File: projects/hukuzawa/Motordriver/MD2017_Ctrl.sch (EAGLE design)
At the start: 18 parts, among them IC1 PIC16F648, J1 3X2A, Q1 CERALOCK

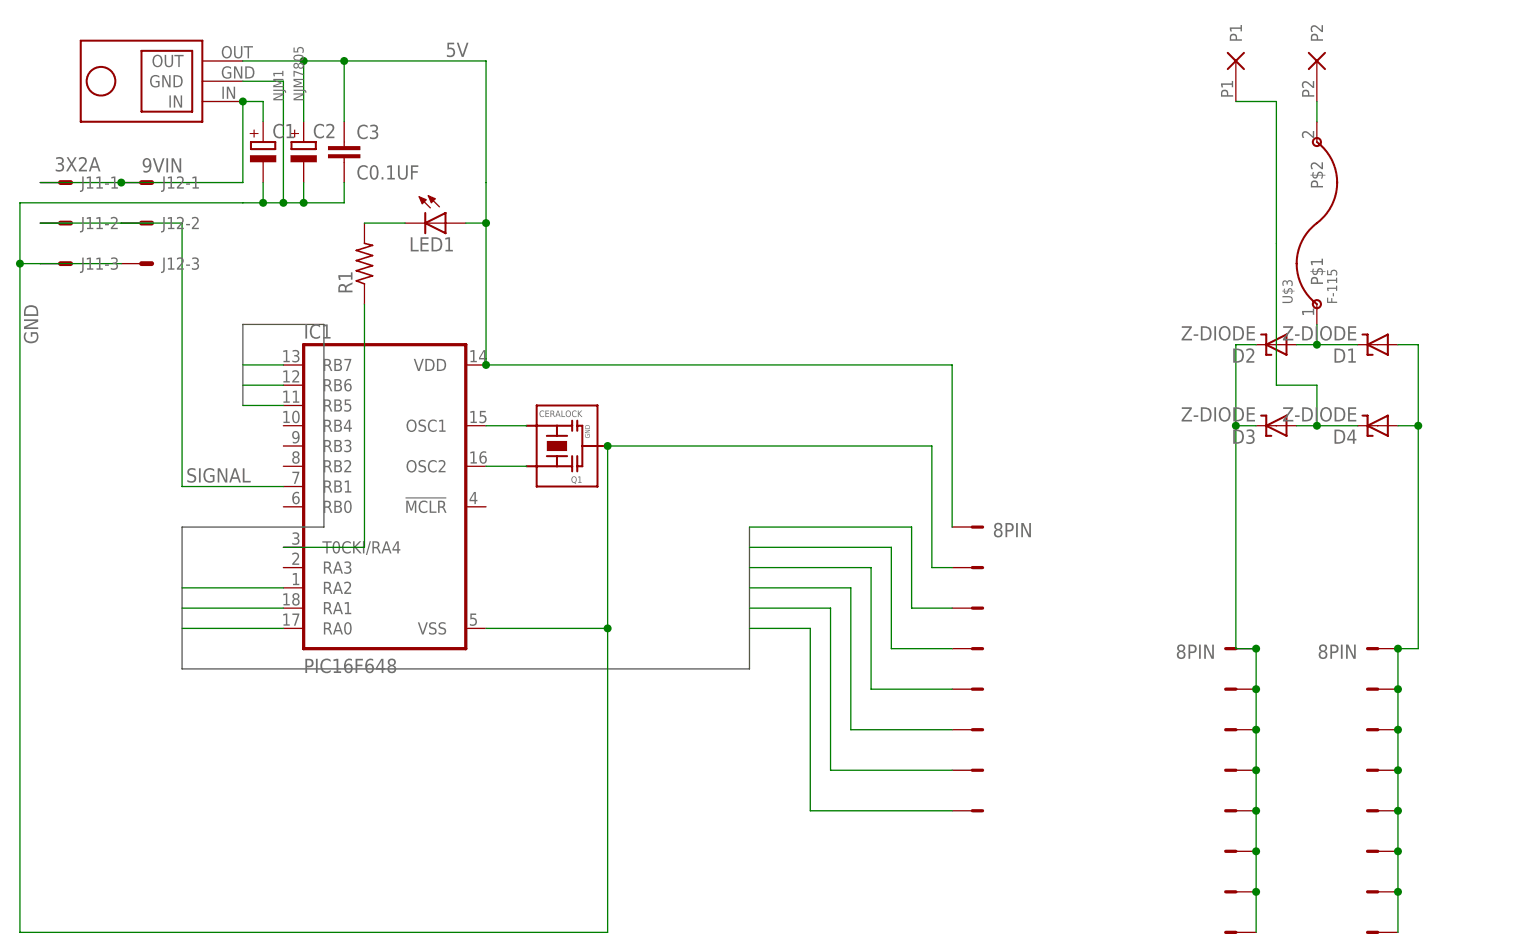
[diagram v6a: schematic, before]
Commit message: モータードライバ全ボード図修正
配置の基準単位をmilに変更して再配置・再配線
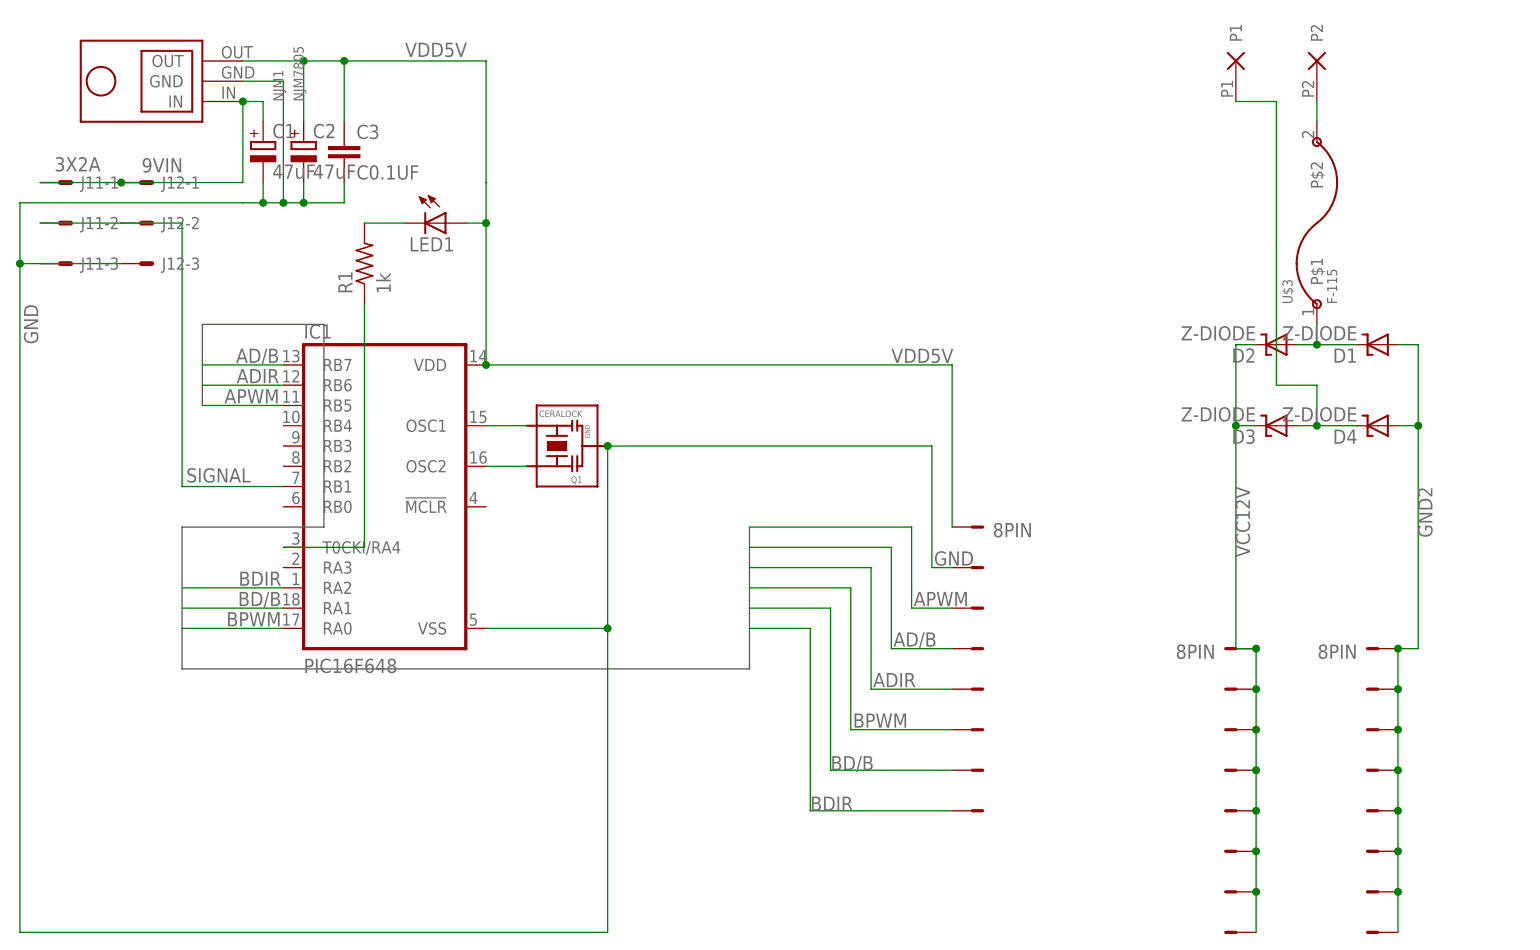
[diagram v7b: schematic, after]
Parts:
- C1, C2: value (none) -> 47uF
- R1: value (none) -> 1k
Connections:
- net 5V renamed VDD5V
- net N$3 renamed GND2
- net N$4 renamed BATTA
- net N$6 renamed BATTB
- net N$7 renamed VCC12V
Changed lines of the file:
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@@
 <part name="J1" library="3M_372xx" deviceset="3X2" device="A"/>
 <part name="LED1" library="FP-21T for MITS" deviceset="LED" device="5MM"/>
-<part name="R1" library="rcl" deviceset="R-US_" device="R3216W"/>
+<part name="R1" library="rcl" deviceset="R-US_" device="R3216W" value="1k"/>
 <part name="U$2" library="Powerio" deviceset="2P" device=""/>
 <part name="U$3" library="testLib" deviceset="F-115" device=""/>
-<part name="C1" library="FP-21T for MITS" deviceset="CPOL-EU2" device="-5MM"/>
-<part name="C2" library="FP-21T for MITS" deviceset="CPOL-EU2" device="-5MM"/>
+<part name="C1" library="FP-21T for MITS" deviceset="CPOL-EU2" device="-5MM" value="47uF"/>
+<part name="C2" library="FP-21T for MITS" deviceset="CPOL-EU2" device="-5MM" value="47uF"/>
 <part name="C3" library="FP-21T for MITS" deviceset="C0.1UF" device=""/>
 <part name="D1" library="diode" deviceset="Z-DIODE" device=""/>
@@
 <bus name="B0">
 <segment>
-<wire x1="-66.04" y1="10.16" x2="-66.04" y2="20.32" width="0.762" layer="92"/>
-<wire x1="-66.04" y1="20.32" x2="-55.88" y2="20.32" width="0.762" layer="92"/>
+<wire x1="-71.12" y1="10.16" x2="-71.12" y2="20.32" width="0.762" layer="92"/>
+<wire x1="-71.12" y1="20.32" x2="-55.88" y2="20.32" width="0.762" layer="92"/>
 <wire x1="-55.88" y1="20.32" x2="-55.88" y2="-5.08" width="0.762" layer="92"/>
 <wire x1="-55.88" y1="-5.08" x2="-73.66" y2="-5.08" width="0.762" layer="92"/>
@@
 </segment>
 </net>
-<net name="5V" class="0">
+<net name="VDD5V" class="0">
 <segment>
 <pinref part="IC1" gate="G$1" pin="VDD"/>
 <wire x1="-35.56" y1="38.1" x2="-35.56" y2="33.02" width="0.1524" layer="91"/>
-<label x="-40.64" y="53.848" size="1.778" layer="95"/>
+<label x="-45.72" y="53.848" size="1.778" layer="95"/>
 <pinref part="LED1" gate="G$1" pin="A"/>
 <wire x1="-35.56" y1="33.02" x2="-35.56" y2="15.24" width="0.1524" layer="91"/>
@@
 <junction x="-53.34" y="53.34"/>
 <junction x="-35.56" y="33.02"/>
+<label x="15.24" y="15.494" size="1.778" layer="95"/>
 </segment>
 </net>
@@
 <junction x="-58.42" y="35.56"/>
 <junction x="-60.96" y="35.56"/>
+<label x="20.574" y="-9.906" size="1.778" layer="95"/>
 </segment>
 </net>
@@
 <pinref part="SIGNALPORT" gate="-3" pin="P$1"/>
 <wire x1="17.78" y1="-15.24" x2="22.86" y2="-15.24" width="0.1524" layer="91"/>
+<label x="18.034" y="-14.986" size="1.778" layer="95"/>
 </segment>
 <segment>
 <pinref part="IC1" gate="G$1" pin="RB5"/>
-<wire x1="-66.04" y1="10.16" x2="-60.96" y2="10.16" width="0.1524" layer="91"/>
+<wire x1="-71.12" y1="10.16" x2="-60.96" y2="10.16" width="0.1524" layer="91"/>
+<label x="-61.468" y="10.414" size="1.778" layer="95" rot="MR0"/>
 </segment>
 </net>
@@
 <pinref part="SIGNALPORT" gate="-4" pin="P$1"/>
 <wire x1="15.24" y1="-20.32" x2="22.86" y2="-20.32" width="0.1524" layer="91"/>
+<label x="15.494" y="-20.066" size="1.778" layer="95"/>
 </segment>
 <segment>
 <pinref part="IC1" gate="G$1" pin="RB7"/>
-<wire x1="-66.04" y1="15.24" x2="-60.96" y2="15.24" width="0.1524" layer="91"/>
+<wire x1="-71.12" y1="15.24" x2="-60.96" y2="15.24" width="0.1524" layer="91"/>
+<label x="-61.468" y="15.494" size="1.778" layer="95" rot="MR0"/>
 </segment>
 </net>
@@
 <pinref part="SIGNALPORT" gate="-5" pin="P$1"/>
 <wire x1="12.7" y1="-25.4" x2="22.86" y2="-25.4" width="0.1524" layer="91"/>
+<label x="12.954" y="-25.146" size="1.778" layer="95"/>
 </segment>
 <segment>
 <pinref part="IC1" gate="G$1" pin="RB6"/>
-<wire x1="-66.04" y1="12.7" x2="-60.96" y2="12.7" width="0.1524" layer="91"/>
+<wire x1="-71.12" y1="12.7" x2="-60.96" y2="12.7" width="0.1524" layer="91"/>
+<label x="-61.468" y="12.954" size="1.778" layer="95" rot="MR0"/>
 </segment>
 </net>
@@
 <pinref part="SIGNALPORT" gate="-6" pin="P$1"/>
 <wire x1="10.16" y1="-30.48" x2="22.86" y2="-30.48" width="0.1524" layer="91"/>
+<label x="10.414" y="-30.226" size="1.778" layer="95"/>
 </segment>
 <segment>
 <pinref part="IC1" gate="G$1" pin="RA0"/>
 <wire x1="-73.66" y1="-17.78" x2="-60.96" y2="-17.78" width="0.1524" layer="91"/>
+<label x="-61.214" y="-17.526" size="1.778" layer="95" rot="MR0"/>
 </segment>
 </net>
@@
 <pinref part="SIGNALPORT" gate="-7" pin="P$1"/>
 <wire x1="7.62" y1="-35.56" x2="22.86" y2="-35.56" width="0.1524" layer="91"/>
+<label x="7.62" y="-35.56" size="1.778" layer="95"/>
 </segment>
 <segment>
 <pinref part="IC1" gate="G$1" pin="RA1"/>
 <wire x1="-60.96" y1="-15.24" x2="-73.66" y2="-15.24" width="0.1524" layer="91"/>
+<label x="-61.214" y="-14.986" size="1.778" layer="95" rot="MR0"/>
 </segment>
 </net>
@@
 <pinref part="SIGNALPORT" gate="-8" pin="P$1"/>
 <wire x1="5.08" y1="-40.64" x2="22.86" y2="-40.64" width="0.1524" layer="91"/>
+<label x="5.08" y="-40.64" size="1.778" layer="95"/>
 </segment>
 <segment>
 <pinref part="IC1" gate="G$1" pin="RA2"/>
 <wire x1="-73.66" y1="-12.7" x2="-60.96" y2="-12.7" width="0.1524" layer="91"/>
-</segment>
-</net>
-<net name="N$3" class="0">
+<label x="-61.214" y="-12.446" size="1.778" layer="95" rot="MR0"/>
+</segment>
+</net>
+<net name="GND2" class="0">
 <segment>
 <wire x1="78.74" y1="17.78" x2="81.28" y2="17.78" width="0.1524" layer="91"/>
@@
 <pinref part="D1" gate="1" pin="A"/>
 <pinref part="D4" gate="1" pin="A"/>
+<label x="81.28" y="0" size="1.778" layer="95" rot="R270"/>
 </segment>
 </net>
@@
 </segment>
 </net>
-<net name="N$6" class="0">
+<net name="BATTB" class="0">
 <segment>
 <wire x1="73.66" y1="7.62" x2="68.58" y2="7.62" width="0.1524" layer="91"/>
@@
 </segment>
 </net>
-<net name="N$7" class="0">
+<net name="VCC12V" class="0">
 <segment>
 <pinref part="POWERPPORT" gate="-8" pin="P$1"/>
@@
 <pinref part="D2" gate="1" pin="C"/>
 <pinref part="D3" gate="1" pin="C"/>
-</segment>
-</net>
-<net name="N$4" class="0">
+<label x="58.42" y="0" size="1.778" layer="95" rot="R270"/>
+</segment>
+</net>
+<net name="BATTA" class="0">
 <segment>
 <pinref part="U$3" gate="G$1" pin="P$2"/>

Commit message: モータードライバ修正
すべての配線の名前を変更
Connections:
- net N$1 renamed NLED1
- net N$5 renamed NBATT1
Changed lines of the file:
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@@
 </segment>
 </net>
-<net name="N$1" class="0">
+<net name="NLED1" class="0">
 <segment>
 <pinref part="R1" gate="G$1" pin="2"/>
@@
 </segment>
 </net>
-<net name="N$5" class="0">
+<net name="NBATT1" class="0">
 <segment>
 <wire x1="73.66" y1="17.78" x2="68.58" y2="17.78" width="0.1524" layer="91"/>
